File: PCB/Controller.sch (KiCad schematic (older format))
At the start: 12 parts, among them IC501 ATMEGA88-A, P501 PRG, SW501 Time Set, SW502 Alarm Set, SW503 Fast, SW504 Slow, SW505 Auto Time, SW506 Sleep, SW507 Summer Time, SW508 Alarm Enabled

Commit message: Added isolation resistors and corrected the reset connection
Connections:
- net Reset: now also IC501.29 ((PCINT14/~RESET~)PC6), R501.2; no longer C501.1, IC501.18 (AVCC), IC501.4 (VCC), IC501.6 (VCC), P501.2 (P2), R501.1
- new net Vcc: C501.1, IC501.18 (AVCC), IC501.4 (VCC), IC501.6 (VCC), P501.2 (P2), R501.1
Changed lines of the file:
@@
 LIBS:valves
 LIBS:Tfac-Symbols
-LIBS:TfaC-cache
 EELAYER 25 0
 EELAYER END
@@
 	1    0    0    -1
 $EndComp
-Text HLabel 2200 2200 0    60   Input ~ 0
+Text HLabel 3100 2200 0    60   Input ~ 0
 Vcc
 Text HLabel 6000 2500 2    60   Input ~ 0
@@
 Text GLabel 6500 1400 0    60   Input ~ 0
 Reset
-Text GLabel 3050 1950 0    60   Input ~ 0
+Text GLabel 6900 3400 2    60   Input ~ 0
 Reset
 $Comp
@@
 	3750 4300 3450 4300
 Wire Wire Line
-	3450 4300 3450 4800
+	3450 4300 3450 4400
+Wire Wire Line
+	3450 4400 3450 4500
+Wire Wire Line
+	3450 4500 3450 4800
 Wire Wire Line
 	3750 4400 3450 4400
@@
 Connection ~ 3450 4500
 Wire Wire Line
-	3600 2200 3600 2500
+	3600 2200 3600 2300
+Wire Wire Line
+	3600 2300 3600 2500
 Wire Wire Line
 	3600 2300 3750 2300
@@
 	6500 1400 7100 1400
 Wire Wire Line
-	10100 1750 10100 5850
+	10100 1750 10100 2200
+Wire Wire Line
+	10100 2200 10100 2650
+Wire Wire Line
+	10100 2650 10100 3100
+Wire Wire Line
+	10100 3100 10100 3800
+Wire Wire Line
+	10100 3800 10100 4350
+Wire Wire Line
+	10100 4350 10100 4800
+Wire Wire Line
+	10100 4800 10100 5650
+Wire Wire Line
+	10100 5650 10100 5850
 Connection ~ 10100 3800
 Wire Wire Line
@@
 	9050 1650 8950 1650
 Wire Wire Line
-	8950 1650 8950 1850
+	8950 1650 8950 1750
+Wire Wire Line
+	8950 1750 8950 1850
 Wire Wire Line
 	8950 1850 9050 1850
@@
 	9550 1650 9650 1650
 Wire Wire Line
-	9650 1650 9650 1850
+	9650 1650 9650 1750
+Wire Wire Line
+	9650 1750 9650 1850
 Wire Wire Line
 	9650 1850 9550 1850
@@
 	9050 2100 8950 2100
 Wire Wire Line
-	8950 2100 8950 2300
+	8950 2100 8950 2200
+Wire Wire Line
+	8950 2200 8950 2300
 Wire Wire Line
 	8950 2300 9050 2300
@@
 	9550 2100 9650 2100
 Wire Wire Line
-	9650 2100 9650 2300
+	9650 2100 9650 2200
+Wire Wire Line
+	9650 2200 9650 2300
 Wire Wire Line
 	9650 2300 9550 2300
@@
 	9050 2550 8950 2550
 Wire Wire Line
-	8950 2550 8950 2750
+	8950 2550 8950 2650
+Wire Wire Line
+	8950 2650 8950 2750
 Wire Wire Line
 	8950 2750 9050 2750
@@
 	9550 2550 9650 2550
 Wire Wire Line
-	9650 2550 9650 2750
+	9650 2550 9650 2650
+Wire Wire Line
+	9650 2650 9650 2750
 Wire Wire Line
 	9650 2750 9550 2750
@@
 	9050 3000 8950 3000
 Wire Wire Line
-	8950 3000 8950 3200
+	8950 3000 8950 3100
+Wire Wire Line
+	8950 3100 8950 3200
 Wire Wire Line
 	8950 3200 9050 3200
@@
 	9550 3000 9650 3000
 Wire Wire Line
-	9650 3000 9650 3200
+	9650 3000 9650 3100
+Wire Wire Line
+	9650 3100 9650 3200
 Wire Wire Line
 	9650 3200 9550 3200
@@
 	9050 4250 8900 4250
 Wire Wire Line
-	8900 4250 8900 4450
+	8900 4250 8900 4350
+Wire Wire Line
+	8900 4350 8900 4450
 Wire Wire Line
 	8900 4450 9050 4450
@@
 	9550 4250 9650 4250
 Wire Wire Line
-	9650 4250 9650 4450
+	9650 4250 9650 4350
+Wire Wire Line
+	9650 4350 9650 4450
 Wire Wire Line
 	9650 4450 9550 4450
@@
 NoConn ~ 9300 3850
 Wire Wire Line
-	2200 2200 3750 2200
-Wire Wire Line
-	5650 3650 6400 3650
+	3100 2200 3350 2200
+Wire Wire Line
+	3350 2200 3600 2200
+Wire Wire Line
+	3600 2200 3750 2200
+Wire Wire Line
+	5650 3650 6100 3650
+Wire Wire Line
+	6100 3650 6400 3650
 Wire Wire Line
 	6700 3650 6900 3650
@@
 	3350 2350 3350 2200
 Connection ~ 3350 2200
-Wire Wire Line
-	3050 1950 3200 1950
-Wire Wire Line
-	3200 1950 3200 2200
-Connection ~ 3200 2200
 Text HLabel 6900 3650 2    60   Input ~ 0
 Vcc
+Wire Wire Line
+	6900 3400 6100 3400
+Wire Wire Line
+	6100 3400 6100 3650
+Connection ~ 6100 3650
 $EndSCHEMATC

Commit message: Trying out an alternative layout
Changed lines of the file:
@@
 $EndComp
 $Comp
-L GND #PWR09
+L GND #PWR502
 U 1 1 5560D64D
 P 3450 4800
-F 0 "#PWR09" H 3450 4550 50  0001 C CNN
+F 0 "#PWR502" H 3450 4550 50  0001 C CNN
 F 1 "GND" H 3450 4650 50  0000 C CNN
 F 2 "" H 3450 4800 60  0000 C CNN
@@
 Vcc
 $Comp
-L GND #PWR010
+L GND #PWR503
 U 1 1 5570FE29
 P 7850 1650
-F 0 "#PWR010" H 7850 1400 50  0001 C CNN
+F 0 "#PWR503" H 7850 1400 50  0001 C CNN
 F 1 "GND" H 7850 1500 50  0000 C CNN
 F 2 "" H 7850 1650 60  0000 C CNN
@@
 $EndComp
 $Comp
-L GND #PWR011
+L GND #PWR501
 U 1 1 55710077
 P 3350 2900
-F 0 "#PWR011" H 3350 2650 50  0001 C CNN
+F 0 "#PWR501" H 3350 2650 50  0001 C CNN
 F 1 "GND" H 3350 2750 50  0000 C CNN
 F 2 "" H 3350 2900 60  0000 C CNN
@@
 Reset
 $Comp
-L GND #PWR012
+L GND #PWR504
 U 1 1 55C0F9DC
 P 10100 5850
-F 0 "#PWR012" H 10100 5600 50  0001 C CNN
+F 0 "#PWR504" H 10100 5600 50  0001 C CNN
 F 1 "GND" H 10100 5700 50  0000 C CNN
 F 2 "" H 10100 5850 60  0000 C CNN
@@
 	3750 4300 3450 4300
 Wire Wire Line
-	3450 4300 3450 4400
-Wire Wire Line
-	3450 4400 3450 4500
-Wire Wire Line
-	3450 4500 3450 4800
+	3450 4300 3450 4800
 Wire Wire Line
 	3750 4400 3450 4400
@@
 Connection ~ 3450 4500
 Wire Wire Line
-	3600 2200 3600 2300
-Wire Wire Line
-	3600 2300 3600 2500
+	3600 2200 3600 2500
 Wire Wire Line
 	3600 2300 3750 2300
@@
 	6500 1400 7100 1400
 Wire Wire Line
-	10100 1750 10100 2200
-Wire Wire Line
-	10100 2200 10100 2650
-Wire Wire Line
-	10100 2650 10100 3100
-Wire Wire Line
-	10100 3100 10100 3800
-Wire Wire Line
-	10100 3800 10100 4350
-Wire Wire Line
-	10100 4350 10100 4800
-Wire Wire Line
-	10100 4800 10100 5650
-Wire Wire Line
-	10100 5650 10100 5850
+	10100 1750 10100 5850
 Connection ~ 10100 3800
 Wire Wire Line
@@
 	9050 1650 8950 1650
 Wire Wire Line
-	8950 1650 8950 1750
-Wire Wire Line
-	8950 1750 8950 1850
+	8950 1650 8950 1850
 Wire Wire Line
 	8950 1850 9050 1850
@@
 	9550 1650 9650 1650
 Wire Wire Line
-	9650 1650 9650 1750
-Wire Wire Line
-	9650 1750 9650 1850
+	9650 1650 9650 1850
 Wire Wire Line
 	9650 1850 9550 1850
@@
 	9050 2100 8950 2100
 Wire Wire Line
-	8950 2100 8950 2200
-Wire Wire Line
-	8950 2200 8950 2300
+	8950 2100 8950 2300
 Wire Wire Line
 	8950 2300 9050 2300
@@
 	9550 2100 9650 2100
 Wire Wire Line
-	9650 2100 9650 2200
-Wire Wire Line
-	9650 2200 9650 2300
+	9650 2100 9650 2300
 Wire Wire Line
 	9650 2300 9550 2300
@@
 	9050 2550 8950 2550
 Wire Wire Line
-	8950 2550 8950 2650
-Wire Wire Line
-	8950 2650 8950 2750
+	8950 2550 8950 2750
 Wire Wire Line
 	8950 2750 9050 2750
@@
 	9550 2550 9650 2550
 Wire Wire Line
-	9650 2550 9650 2650
-Wire Wire Line
-	9650 2650 9650 2750
+	9650 2550 9650 2750
 Wire Wire Line
 	9650 2750 9550 2750
@@
 	9050 3000 8950 3000
 Wire Wire Line
-	8950 3000 8950 3100
-Wire Wire Line
-	8950 3100 8950 3200
+	8950 3000 8950 3200
 Wire Wire Line
 	8950 3200 9050 3200
@@
 	9550 3000 9650 3000
 Wire Wire Line
-	9650 3000 9650 3100
-Wire Wire Line
-	9650 3100 9650 3200
+	9650 3000 9650 3200
 Wire Wire Line
 	9650 3200 9550 3200
@@
 	9050 4250 8900 4250
 Wire Wire Line
-	8900 4250 8900 4350
-Wire Wire Line
-	8900 4350 8900 4450
+	8900 4250 8900 4450
 Wire Wire Line
 	8900 4450 9050 4450
@@
 	9550 4250 9650 4250
 Wire Wire Line
-	9650 4250 9650 4350
-Wire Wire Line
-	9650 4350 9650 4450
+	9650 4250 9650 4450
 Wire Wire Line
 	9650 4450 9550 4450
@@
 NoConn ~ 9300 3850
 Wire Wire Line
-	3100 2200 3350 2200
-Wire Wire Line
-	3350 2200 3600 2200
-Wire Wire Line
-	3600 2200 3750 2200
-Wire Wire Line
-	5650 3650 6100 3650
-Wire Wire Line
-	6100 3650 6400 3650
+	3100 2200 3750 2200
+Wire Wire Line
+	5650 3650 6400 3650
 Wire Wire Line
 	6700 3650 6900 3650

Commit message: Added indicator LEDs and Heartbeat
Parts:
- added D501: LED, LEDs:LED-0805, symbol LED
- added R502: 480Ω, Resistors_SMD:R_0805_HandSoldering, symbol R
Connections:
- net GND: now also R502.1
- net Heartbeat: now reaches IC501.12 ((PCINT0/CLKO/ICP1)PB0)
- net Heartbeat: now also D501.2 (A)
- new net: D501.1 (K), R502.2
- no-connect marks 12 -> 11
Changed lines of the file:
@@
 LIBS:valves
 LIBS:Tfac-Symbols
+LIBS:TfaC-cache
 EELAYER 25 0
 EELAYER END
@@
 $EndComp
 $Comp
-L GND #PWR08
+L GND #PWR010
 U 1 1 5560D64D
 P 3450 4800
-F 0 "#PWR08" H 3450 4550 50  0001 C CNN
+F 0 "#PWR010" H 3450 4550 50  0001 C CNN
 F 1 "GND" H 3450 4650 50  0000 C CNN
 F 2 "" H 3450 4800 60  0000 C CNN
@@
 Vcc
 $Comp
-L GND #PWR09
+L GND #PWR011
 U 1 1 5570FE29
 P 7850 1650
-F 0 "#PWR09" H 7850 1400 50  0001 C CNN
+F 0 "#PWR011" H 7850 1400 50  0001 C CNN
 F 1 "GND" H 7850 1500 50  0000 C CNN
 F 2 "" H 7850 1650 60  0000 C CNN
@@
 $EndComp
 $Comp
-L GND #PWR010
+L GND #PWR012
 U 1 1 55710077
 P 3350 2900
-F 0 "#PWR010" H 3350 2650 50  0001 C CNN
+F 0 "#PWR012" H 3350 2650 50  0001 C CNN
 F 1 "GND" H 3350 2750 50  0000 C CNN
 F 2 "" H 3350 2900 60  0000 C CNN
@@
 Reset
 $Comp
-L GND #PWR011
+L GND #PWR013
 U 1 1 55C0F9DC
 P 10100 5850
-F 0 "#PWR011" H 10100 5600 50  0001 C CNN
+F 0 "#PWR013" H 10100 5600 50  0001 C CNN
 F 1 "GND" H 10100 5700 50  0000 C CNN
 F 2 "" H 10100 5850 60  0000 C CNN
@@
 Text GLabel 5900 4400 2    60   Input ~ 0
 Summer_Time
-NoConn ~ 5650 2200
 NoConn ~ 5650 2800
 NoConn ~ 5650 2900
@@
 	6100 3400 6100 3650
 Connection ~ 6100 3650
+$Comp
+L LED D501
+U 1 1 564D7767
+P 6950 2200
+F 0 "D501" H 6950 2300 50  0000 C CNN
+F 1 "LED" H 6950 2100 50  0000 C CNN
+F 2 "LEDs:LED-0805" H 6950 2200 60  0001 C CNN
+F 3 "" H 6950 2200 60  0000 C CNN
+	1    6950 2200
+	-1   0    0    1
+$EndComp
+$Comp
+L R R502
+U 1 1 564D780E
+P 7400 2200
+F 0 "R502" V 7480 2200 50  0000 C CNN
+F 1 "480Ω" V 7300 2200 50  0000 C CNN
+F 2 "Resistors_SMD:R_0805_HandSoldering" V 7330 2200 30  0001 C CNN
+F 3 "" H 7400 2200 30  0000 C CNN
+	1    7400 2200
+	0    1    1    0
+$EndComp
+$Comp
+L GND #PWR014
+U 1 1 564D788E
+P 7700 2300
+F 0 "#PWR014" H 7700 2050 50  0001 C CNN
+F 1 "GND" H 7700 2150 50  0000 C CNN
+F 2 "" H 7700 2300 60  0000 C CNN
+F 3 "" H 7700 2300 60  0000 C CNN
+	1    7700 2300
+	1    0    0    -1
+$EndComp
+Wire Wire Line
+	5650 2200 6750 2200
+Wire Wire Line
+	7150 2200 7250 2200
+Wire Wire Line
+	7550 2200 7700 2200
+Wire Wire Line
+	7700 2200 7700 2300
+Text Label 6000 2200 0    60   ~ 0
+Heartbeat
 $EndSCHEMATC

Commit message: Updated the board for further features to the display
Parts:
- added SW509: Reset, tfac-footprints:PTS525SM15SMTR2LFS, symbol SW_PUSH
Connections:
- net GND: now also SW509.2
- net Reset: now also SW509.1
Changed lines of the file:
@@
 	0    1    1    0
 $EndComp
-Text GLabel 6500 1400 0    60   Input ~ 0
-Reset
-Text GLabel 6900 3400 2    60   Input ~ 0
-Reset
 $Comp
 L GND #PWR013
@@
 Text Label 6000 2200 0    60   ~ 0
 Heartbeat
+Text HLabel 6900 3400 2    60   Input ~ 0
+Reset
+Text HLabel 6500 1400 0    60   Input ~ 0
+Reset
+$Comp
+L SW_PUSH SW509
+U 1 1 5660B19B
+P 6300 5250
+F 0 "SW509" H 5950 5350 50  0000 C CNN
+F 1 "Reset" H 6300 5170 50  0000 C CNN
+F 2 "tfac-footprints:PTS525SM15SMTR2LFS" H 6300 5250 60  0001 C CNN
+F 3 "" H 6300 5250 60  0000 C CNN
+	1    6300 5250
+	1    0    0    -1
+$EndComp
+Text HLabel 5650 5250 0    60   Input ~ 0
+Reset
+Wire Wire Line
+	5650 5250 6000 5250
+$Comp
+L GND #PWR015
+U 1 1 5660B31D
+P 6800 5400
+F 0 "#PWR015" H 6800 5150 50  0001 C CNN
+F 1 "GND" H 6800 5250 50  0000 C CNN
+F 2 "" H 6800 5400 60  0000 C CNN
+F 3 "" H 6800 5400 60  0000 C CNN
+	1    6800 5400
+	1    0    0    -1
+$EndComp
+Wire Wire Line
+	6600 5250 6800 5250
+Wire Wire Line
+	6800 5250 6800 5400
 $EndSCHEMATC

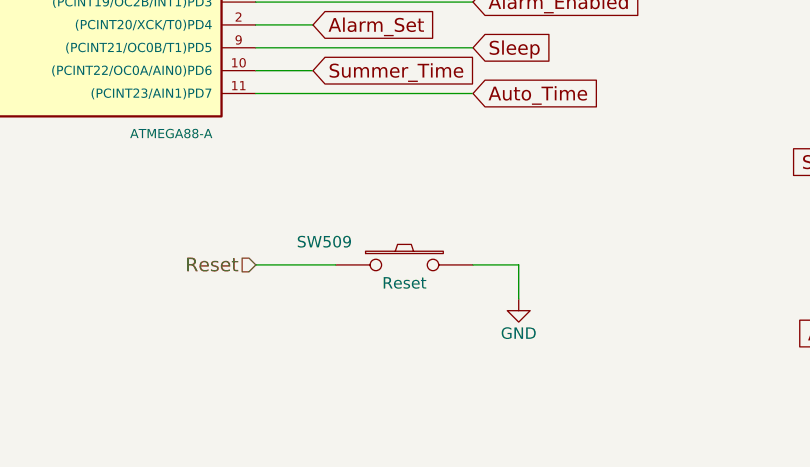
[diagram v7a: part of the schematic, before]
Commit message: Corrected the symbol and footprint for the reset switch
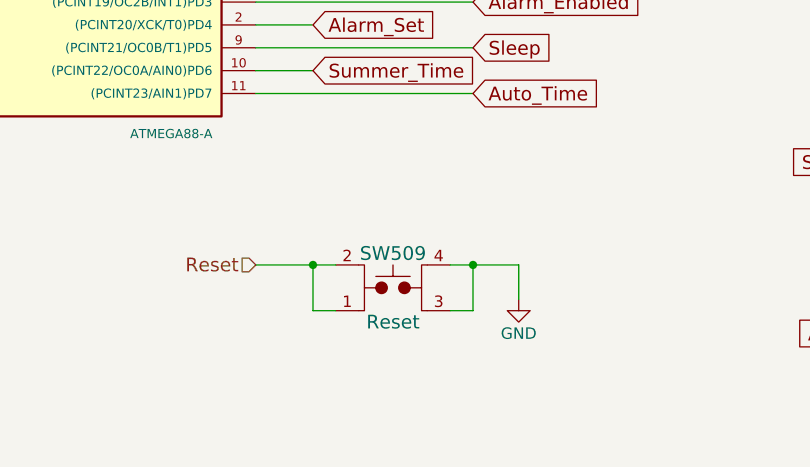
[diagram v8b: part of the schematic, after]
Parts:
- removed SW509: Reset, tfac-footprints:PTS525SM15SMTR2LFS, symbol SW_PUSH
- added SW509: Reset, tfac-footprints:PTS525SM15SMTR2LFS, symbol TL3315NF160Q
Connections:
- net GND: now also SW509.3, SW509.4
- net Reset: now also SW509.1, SW509.2
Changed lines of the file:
@@
 LIBS:valves
 LIBS:Tfac-Symbols
-LIBS:TfaC-cache
 EELAYER 25 0
 EELAYER END
@@
 Text HLabel 6500 1400 0    60   Input ~ 0
 Reset
-$Comp
-L SW_PUSH SW509
-U 1 1 5660B19B
-P 6300 5250
-F 0 "SW509" H 5950 5350 50  0000 C CNN
-F 1 "Reset" H 6300 5170 50  0000 C CNN
-F 2 "tfac-footprints:PTS525SM15SMTR2LFS" H 6300 5250 60  0001 C CNN
-F 3 "" H 6300 5250 60  0000 C CNN
-	1    6300 5250
-	1    0    0    -1
-$EndComp
 Text HLabel 5650 5250 0    60   Input ~ 0
 Reset
@@
 $EndComp
 Wire Wire Line
-	6600 5250 6800 5250
+	6500 5250 6800 5250
 Wire Wire Line
 	6800 5250 6800 5400
+$Comp
+L TL3315NF160Q SW509
+U 1 1 566C6130
+P 6250 5350
+F 0 "SW509" V 6400 5350 60  0000 C CNN
+F 1 "Reset" V 6100 5350 60  0000 C CNN
+F 2 "tfac-footprints:PTS525SM15SMTR2LFS" H 6250 5300 60  0001 C CNN
+F 3 "" H 6250 5300 60  0000 C CNN
+	1    6250 5350
+	0    -1   -1   0
+$EndComp
+Wire Wire Line
+	5900 5250 5900 5450
+Wire Wire Line
+	5900 5450 6000 5450
+Connection ~ 5900 5250
+Wire Wire Line
+	6500 5450 6600 5450
+Wire Wire Line
+	6600 5450 6600 5250
+Connection ~ 6600 5250
 $EndSCHEMATC
